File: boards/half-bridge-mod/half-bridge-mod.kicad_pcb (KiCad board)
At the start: 2 copper layers, 60 x 51 mm, 20 parts, among them J1 Conn_01x04_Male, J2 Conn_01x01_Female, J3 Conn_01x01_Female, J4 Conn_01x01_Female, J5 Conn_01x04_Male, Q1 Q_NIGBT_GCE, Q2 Q_NIGBT_GCE

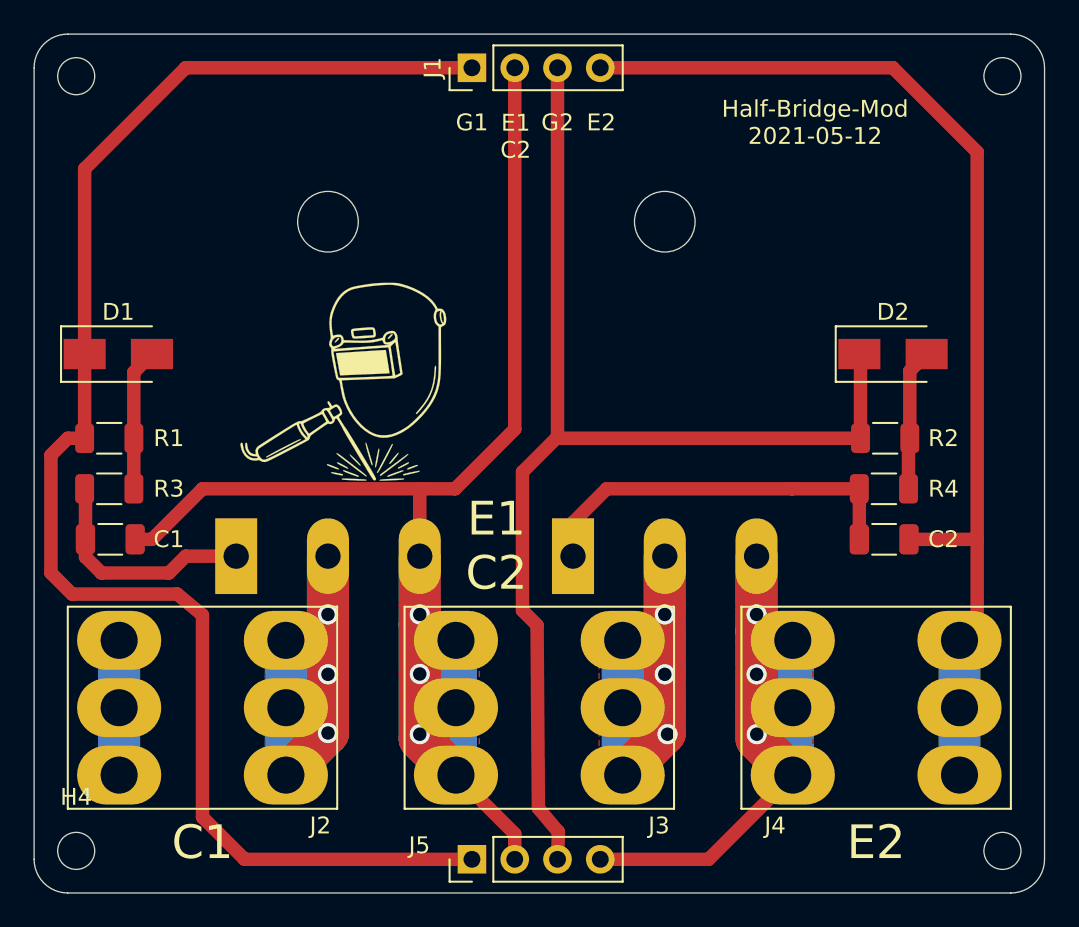
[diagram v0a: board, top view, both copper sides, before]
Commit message: half-bridge-mod: updated to kicad 7
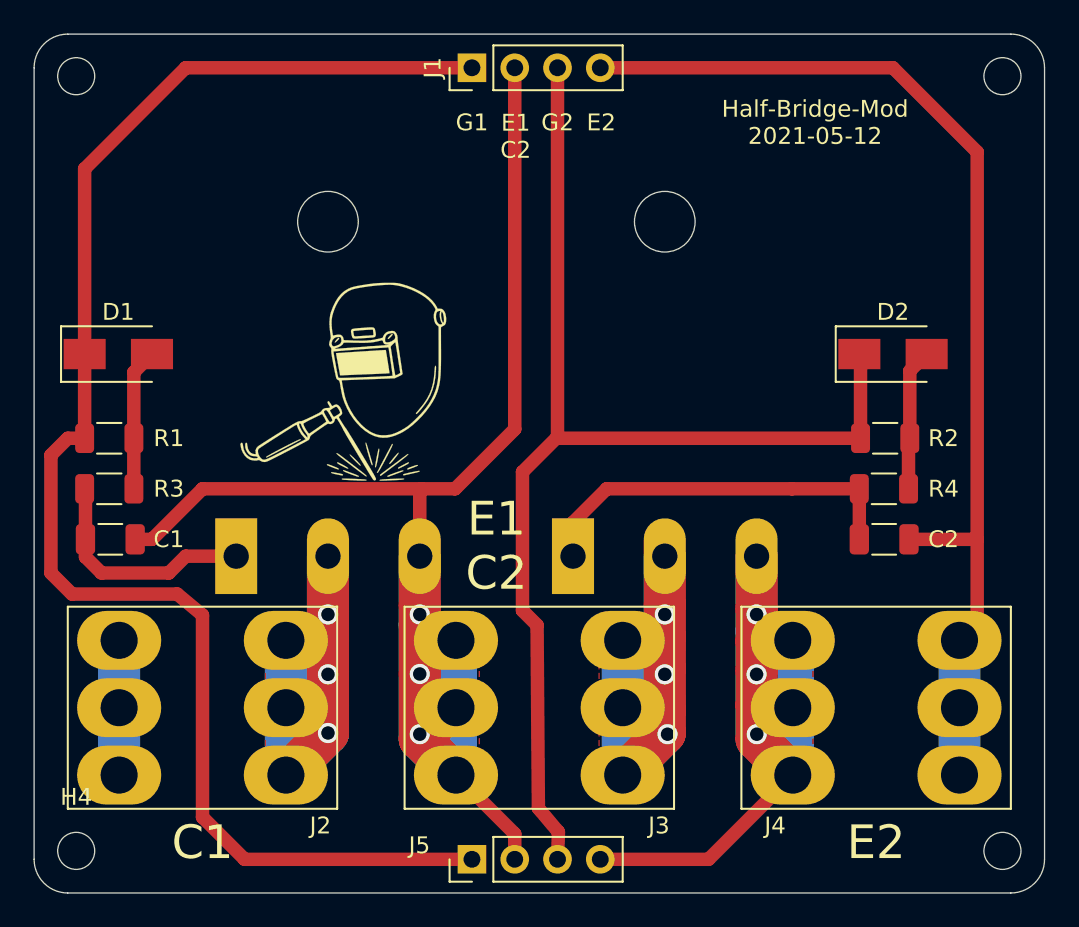
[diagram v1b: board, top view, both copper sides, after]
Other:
- net class Default removed
